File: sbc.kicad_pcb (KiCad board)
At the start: 6 copper layers, 76.2 x 50.8 mm, 159 parts, among them J1 USB_C_Receptacle_USB2.0_14P, J2 Micro_SD_Card, J3 Conn_01x02_Pin, J4 Conn_01x06_Pin, J5 Conn_01x14_Pin, J6 USB_C_Receptacle_USB2.0_14P, J7 USB_C_Receptacle_USB2.0_14P, J8 Conn_01x14_Pin, J9 Conn_01x04_Pin, Q2 BSS84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

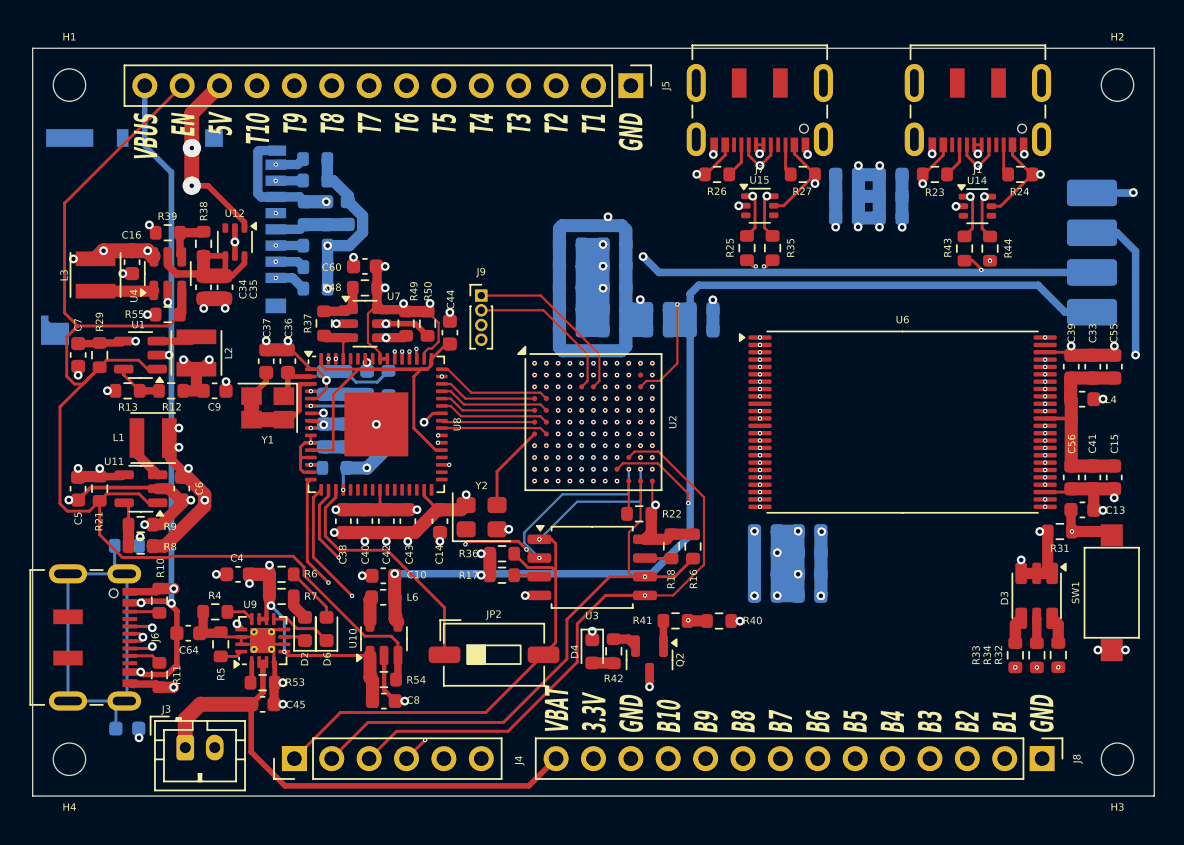
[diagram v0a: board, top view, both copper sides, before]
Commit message: End of Version 1.0. Feedback received
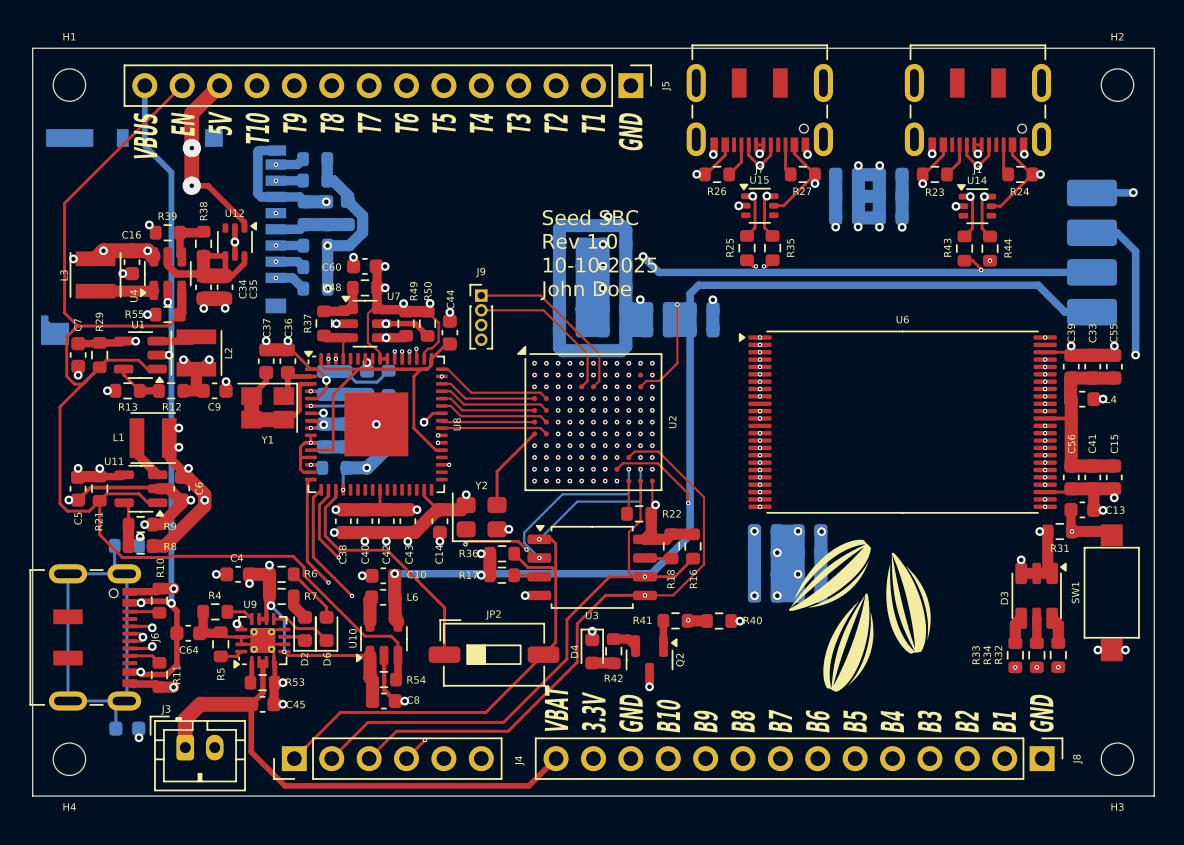
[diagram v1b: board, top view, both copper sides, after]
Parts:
- added G***: LOGO, logos:seeds, F.Cu at (158.1, 114.6)
- FB1: footprint Capacitor_SMD:C_0603_1608Metric -> Inductor_SMD:L_0603_1608Metric
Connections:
- Y1 pad 3: Net-(U8-OSCO) -> (no net)
- Y1 pad 4: Net-(U8-OSCO) -> (no net)
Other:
- board text added: "Seed SBC Rev 1.0 10-10-2025 John Doe"
